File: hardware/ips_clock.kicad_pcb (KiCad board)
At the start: 2 copper layers, 106.9 x 63 mm, 7 parts, among them J1 Conn_02x06_Odd_Even, J2 Conn_02x06_Odd_Even, J3 Conn_02x06_Odd_Even, J4 Conn_02x06_Odd_Even, J5 Conn_02x06_Odd_Even, J6 Conn_02x06_Odd_Even, U1 LUAT-ESP32-C3

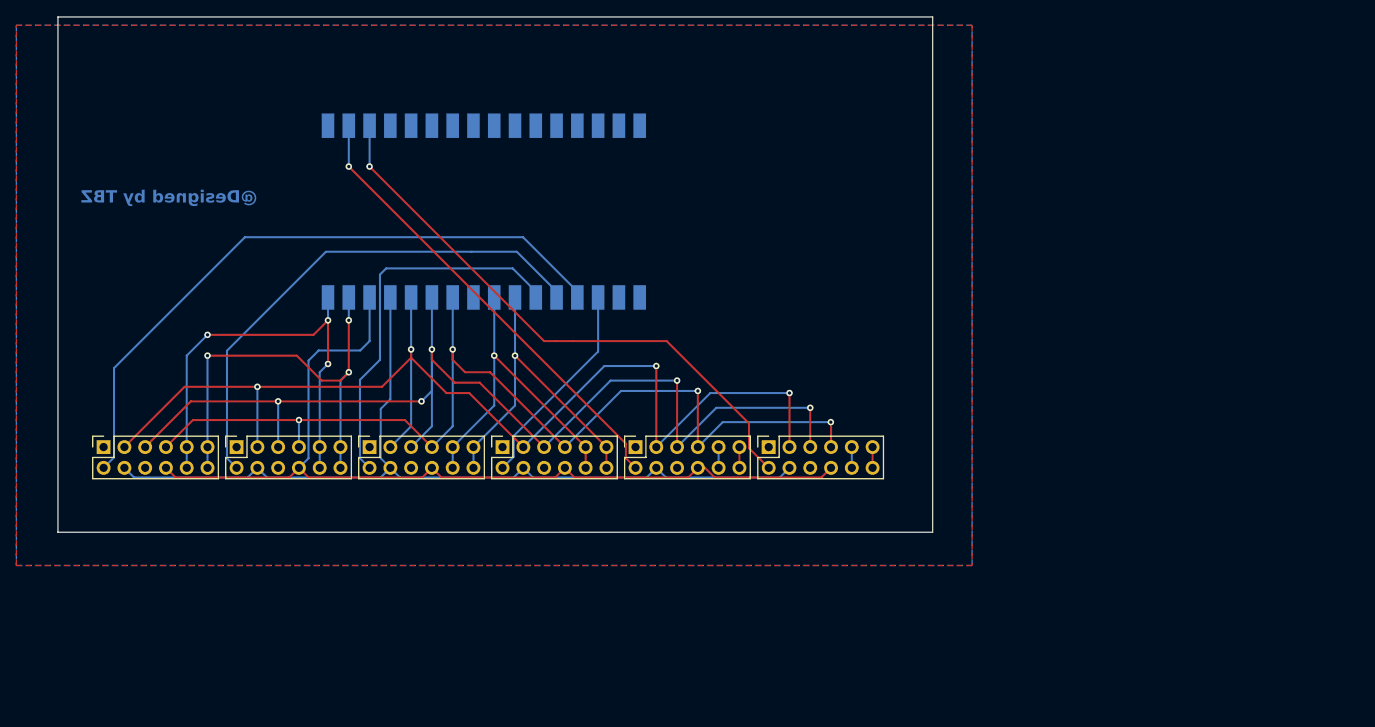
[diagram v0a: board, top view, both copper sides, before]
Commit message: 最后更新了PCB的布局
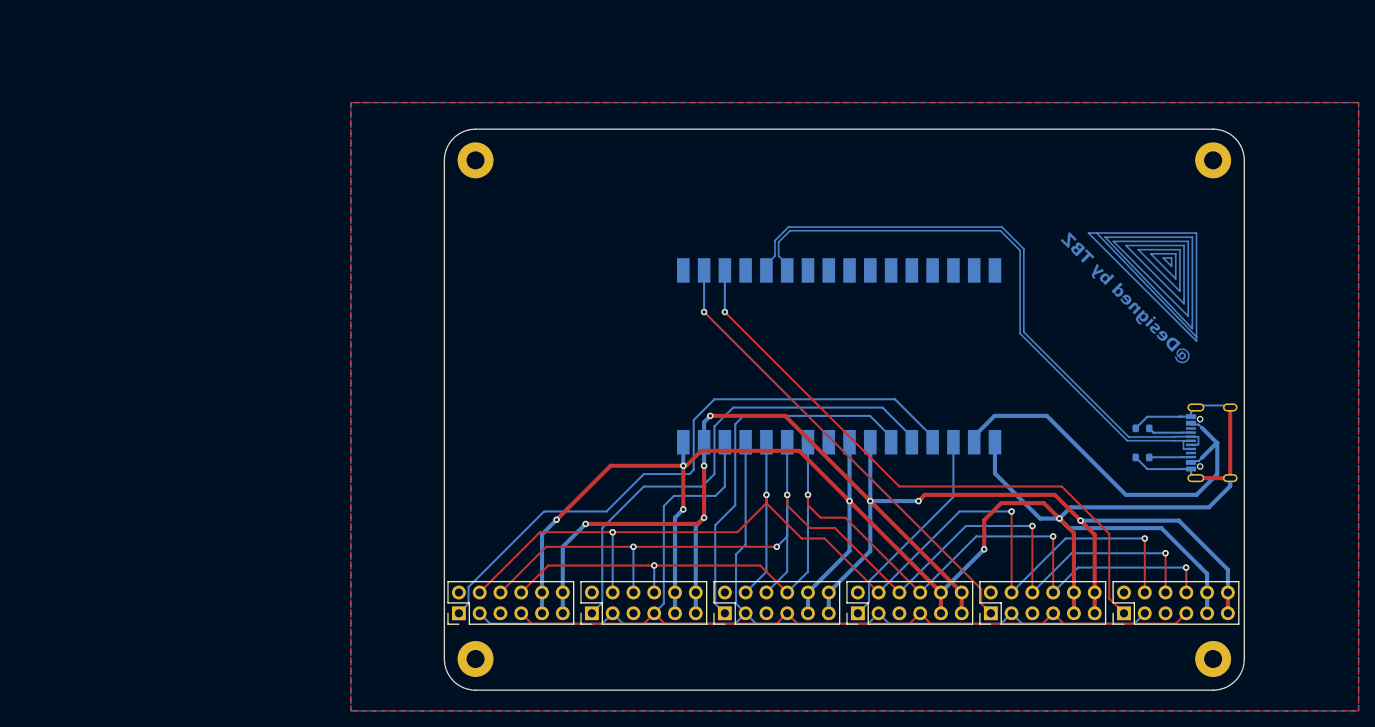
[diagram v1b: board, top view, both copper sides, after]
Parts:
- added H1: MountingHole, MountingHole:MountingHole_2.2mm_M2_Pad, F.Cu at (104.4, 64.8)
- added H2: MountingHole, MountingHole:MountingHole_2.2mm_M2_Pad, F.Cu at (194.6, 64.8)
- added H3: MountingHole, MountingHole:MountingHole_2.2mm_M2_Pad, F.Cu at (104.4, 125.7)
- added H4: MountingHole, MountingHole:MountingHole_2.2mm_M2_Pad, F.Cu at (194.6, 125.7)
- added J7: USB_C_Receptacle_USB2.0, Connector_USB:USB_C_Receptacle_G-Switch_GT-USB-7010ASV, B.Cu at (195.6, 99.3)
- added R1: 5.1K, Resistor_SMD:R_0603_1608Metric, B.Cu at (185.9, 97.5)
- added R2: 5.1K, Resistor_SMD:R_0603_1608Metric, B.Cu at (185.9, 101.1)
- J1, J2, J3, J4, J5, J6: value Conn_02x06_Odd_Even -> Conn_02x06_Top_Bottom; footprint my_connector:PMOD -> my_connector:PMOD-HOST
- moved J4 46.9 mm to (157.5, 118.9)
- moved J6 46.9 mm to (190.0, 118.9)
- moved J2 46.9 mm to (125.0, 118.9)
- moved J5 46.9 mm to (173.7, 118.9)
- moved J3 46.9 mm to (141.2, 118.9)
- moved J1 46.9 mm to (108.7, 118.9)
- moved U1 46.8 mm to (148.3, 88.7)
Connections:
- J1 pad 1: /ips_lcd1/INT -> /CS1
- J1 pad 10: GND -> /BLK
- J1 pad 11: +3V3 -> GND
- J1 pad 2: /CS1 -> /SDA
- J1 pad 3: /RST -> /ips_lcd1/MISO
- J1 pad 4: /SDA -> /SCL
- J1 pad 5: /DC -> GND
- J1 pad 6: /ips_lcd1/MISO -> +3V3
- J1 pad 7: /BLK -> /ips_lcd1/INT
- J1 pad 8: /SCL -> /RST
- J1 pad 9: GND -> /DC
- J2 pad 1: /ips_lcd2/INT -> /CS2
- J2 pad 10: GND -> /BLK
- J2 pad 11: +3V3 -> GND
- J2 pad 2: /CS2 -> /SDA
- J2 pad 3: /RST -> /ips_lcd2/MISO
- J2 pad 4: /SDA -> /SCL
- J2 pad 5: /DC -> GND
- J2 pad 6: /ips_lcd2/MISO -> +3V3
- J2 pad 7: /BLK -> /ips_lcd2/INT
- J2 pad 8: /SCL -> /RST
- J2 pad 9: GND -> /DC
- J3 pad 1: /ips_lcd3/INT -> /CS3
- J3 pad 10: GND -> /BLK
- J3 pad 11: +3V3 -> GND
- J3 pad 2: /CS3 -> /SDA
- J3 pad 3: /RST -> /ips_lcd3/MISO
- J3 pad 4: /SDA -> /SCL
- J3 pad 5: /DC -> GND
- J3 pad 6: /ips_lcd3/MISO -> +3V3
- J3 pad 7: /BLK -> /ips_lcd3/INT
- J3 pad 8: /SCL -> /RST
- J3 pad 9: GND -> /DC
- J4 pad 1: /ips_lcd4/INT -> /CS4
- J4 pad 10: GND -> /BLK
- J4 pad 11: +3V3 -> GND
- J4 pad 2: /CS4 -> /SDA
- J4 pad 3: /RST -> /ips_lcd4/MISO
- J4 pad 4: /SDA -> /SCL
- J4 pad 5: /DC -> GND
- J4 pad 6: /ips_lcd4/MISO -> +3V3
- J4 pad 7: /BLK -> /ips_lcd4/INT
- J4 pad 8: /SCL -> /RST
- J4 pad 9: GND -> /DC
- J5 pad 1: /ips_lcd5/INT -> /CS5
- J5 pad 10: GND -> /BLK
- J5 pad 11: +3V3 -> GND
- J5 pad 2: /CS5 -> /SDA
- J5 pad 3: /RST -> /ips_lcd5/MISO
- J5 pad 4: /SDA -> /SCL
- J5 pad 5: /DC -> GND
- J5 pad 6: /ips_lcd5/MISO -> +3V3
- J5 pad 7: /BLK -> /ips_lcd5/INT
- J5 pad 8: /SCL -> /RST
- J5 pad 9: GND -> /DC
- J6 pad 1: /ips_lcd6/INT -> /CS6
- J6 pad 10: GND -> /BLK
- J6 pad 11: +3V3 -> GND
- J6 pad 2: /CS6 -> /SDA
- J6 pad 3: /RST -> /ips_lcd6/MISO
- J6 pad 4: /SDA -> /SCL
- J6 pad 5: /DC -> GND
- J6 pad 6: /ips_lcd6/MISO -> +3V3
- J6 pad 7: /BLK -> /ips_lcd6/INT
- J6 pad 8: /SCL -> /RST
- J6 pad 9: GND -> /DC
- U1 pad 5: unconnected-(U1-GPIO18/USB_D--Pad5) -> /UD-
- U1 pad 6: unconnected-(U1-GPIO19/USB_D+-Pad6) -> /UD+
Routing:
- net GND: track 100.4 -> 248.9 mm, vias 4 -> 6
- net +3V3: track 100.3 -> 182.1 mm, vias 4 -> 7
- net /UD-: track 0.00 -> 74.9 mm
- net /UD+: track 0.00 -> 74.2 mm
- net +5V: track 0.00 -> 48.7 mm
- net Net-(J7-CC1): track 0.00 -> 5.33 mm
- net Net-(J7-CC2): track 0.00 -> 5.12 mm
- net /CS1: track 79.5 -> 76.1 mm
- net /CS6: track 70.8 -> 73.7 mm
- net /CS2: track 62.8 -> 60.5 mm
- net /CS3: track 46.4 -> 45.9 mm
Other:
- board size 106.9 x 63 mm -> 97.8 x 68.6 mm
- board text added: "LUATOS-ESP32C3"
- board text added: "M2"
- board text added: "jlcjlcjlcjlc"
- board text added: "关于屏幕的资料可以访问以下链接获得 https://github.com/TheBadZhang/ips_clock"
- board text added: "屏幕 1"
- board text added: "屏幕 2"
- board text added: "屏幕 3"
- board text added: "屏幕 4"
- board text added: "屏幕 5"
- board text added: "屏幕 6"
- board text added: "简易基于ESP32C3设计的物联网时钟，@Design By TheBadZhang"
